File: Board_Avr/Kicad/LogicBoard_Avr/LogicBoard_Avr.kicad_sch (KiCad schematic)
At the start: 11 parts, among them J11 TriggeredStatusLedConnector, SW1 Reset switch, U1 ATmega328PB-A

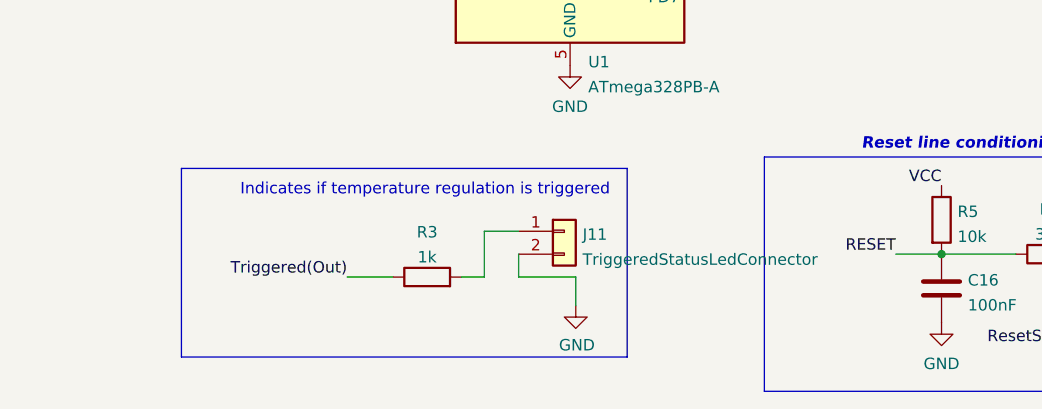
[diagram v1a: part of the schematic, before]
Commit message: Tweaked top silkscreen to embed useful information
Signed-off-by: bebenlebricolo <benoittarrade@hotmail.fr>
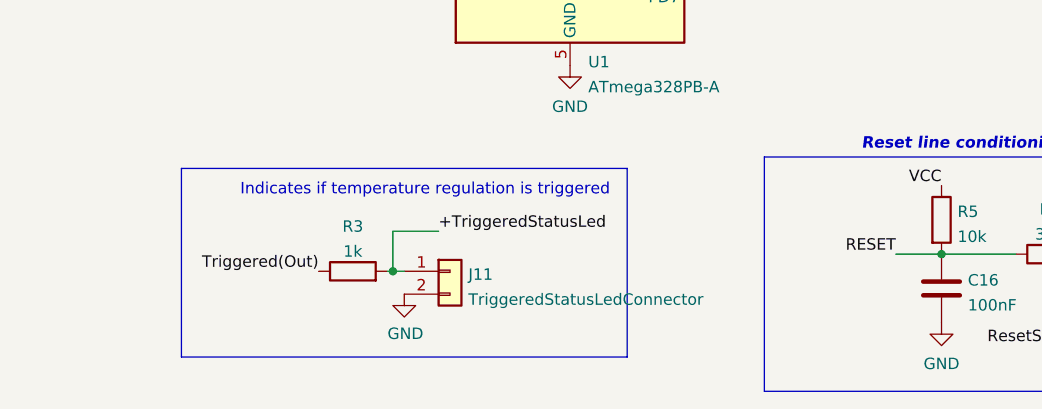
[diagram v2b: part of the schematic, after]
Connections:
- net +TriggeredStatusLed: now reaches J11.1 (Pin_1), R3.2
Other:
- moved on the sheet: J11, R3
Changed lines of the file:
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@@
 (kicad_sch (version 20211123) (generator eeschema)
   (paper "A4")
+  (junction (at 41.91 174.625) (diameter 0) (color 0 0 0 0)
+  )
   (junction (at 122.428 172.72) (diameter 0) (color 0 0 0 0)
   )
@@
     (stroke (width 0) (type default) (color 0 0 0 0))
   )
-  (wire (pts (xy 52.07 175.26) (xy 52.07 170.18))
-    (stroke (width 0) (type default) (color 0 0 0 0))
-  )
   (wire (pts (xy 256.032 77.47) (xy 259.588 77.47))
     (stroke (width 0) (type default) (color 0 0 0 0))
@@
     (stroke (width 0) (type solid) (color 0 0 0 0))
   )
-  (wire (pts (xy 52.07 170.18) (xy 55.88 170.18))
-    (stroke (width 0) (type default) (color 0 0 0 0))
-  )
   (polyline (pts (xy 242.443 46.101) (xy 242.443 42.291))
     (stroke (width 0) (type default) (color 0 0 0 0))
@@
     (stroke (width 0) (type default) (color 0 0 0 0))
   )
-  (wire (pts (xy 55.88 172.72) (xy 55.88 175.26))
-    (stroke (width 0) (type default) (color 0 0 0 0))
-  )
   (wire (pts (xy 207.645 104.775) (xy 213.487 104.775))
     (stroke (width 0) (type default) (color 0 0 0 0))
@@
     (stroke (width 0) (type default) (color 0 0 0 0))
   )
-  (wire (pts (xy 62.23 175.26) (xy 62.23 178.435))
-    (stroke (width 0) (type default) (color 0 0 0 0))
-  )
   (wire (pts (xy 213.233 53.086) (xy 206.883 53.086))
     (stroke (width 0) (type default) (color 0 0 0 0))
@@
     (stroke (width 0) (type default) (color 0 0 0 0))
   )
-  (wire (pts (xy 49.53 175.26) (xy 52.07 175.26))
-    (stroke (width 0) (type default) (color 0 0 0 0))
-  )
   (polyline (pts (xy 27.178 133.096) (xy 33.528 133.096))
     (stroke (width 0) (type solid) (color 0 0 0 0))
@@
     (stroke (width 0) (type default) (color 0 0 0 0))
   )
-  (wire (pts (xy 55.88 175.26) (xy 62.23 175.26))
+  (wire (pts (xy 41.275 174.625) (xy 41.91 174.625))
     (stroke (width 0) (type default) (color 0 0 0 0))
   )
@@
     (stroke (width 0) (type default) (color 0 0 0 0))
   )
-  (wire (pts (xy 36.83 175.26) (xy 41.91 175.26))
-    (stroke (width 0) (type default) (color 0 0 0 0))
-  )
   (wire (pts (xy 213.487 104.775) (xy 213.995 104.775))
     (stroke (width 0) (type default) (color 0 0 0 0))
@@
     (stroke (width 0) (type default) (color 0 0 0 0))
   )
+  (wire (pts (xy 41.91 174.625) (xy 43.18 174.625))
+    (stroke (width 0) (type default) (color 0 0 0 0))
+  )
   (wire (pts (xy 64.135 64.77) (xy 64.135 75.565))
     (stroke (width 0) (type default) (color 0 0 0 0))
@@
     (stroke (width 0) (type default) (color 0 0 0 0))
   )
+  (wire (pts (xy 41.91 170.18) (xy 46.99 170.18))
+    (stroke (width 0) (type default) (color 0 0 0 0))
+  )
   (polyline (pts (xy 87.63 133.096) (xy 95.758 133.096))
     (stroke (width 0) (type solid) (color 0 0 0 0))
@@
   )
   (wire (pts (xy 61.595 64.77) (xy 61.595 75.565))
+    (stroke (width 0) (type default) (color 0 0 0 0))
+  )
+  (wire (pts (xy 41.91 170.18) (xy 41.91 174.625))
     (stroke (width 0) (type default) (color 0 0 0 0))
   )
@@
     (effects (font (size 1.27 1.27)) (justify left bottom))
   )
-  (label "Triggered(Out)" (at 36.83 175.26 180)
+  (label "Triggered(Out)" (at 33.655 174.625 180)
     (effects (font (size 1.27 1.27)) (justify right bottom))
   )
@@
   (label "RESET" (at 97.79 172.72 180)
     (effects (font (size 1.27 1.27)) (justify right bottom))
+  )
+  (label "+TriggeredStatusLed" (at 46.99 170.18 0)
+    (effects (font (size 1.27 1.27)) (justify left bottom))
   )
   (label "MISO0(Prog)" (at 76.835 93.345 0)
@@
     (pin "2")
   )
-  (symbol (lib_id "power:GND") (at 62.23 178.435 0) (unit 1)
+  (symbol (lib_id "power:GND") (at 43.18 177.165 0) (unit 1)
     (in_bom yes) (on_board yes)
-    (property "Reference" "#PWR014" (id 0) (at 62.23 184.785 0)
-      (effects (font (size 1.27 1.27)) hide)
-    )
-    (property "Value" "GND" (id 1) (at 62.357 182.8292 0))
-    (property "Footprint" "" (id 2) (at 62.23 178.435 0)
-      (effects (font (size 1.27 1.27)) hide)
-    )
-    (property "Datasheet" "" (id 3) (at 62.23 178.435 0)
+    (property "Reference" "#PWR014" (id 0) (at 43.18 183.515 0)
+      (effects (font (size 1.27 1.27)) hide)
+    )
+    (property "Value" "GND" (id 1) (at 43.307 181.5592 0))
+    (property "Footprint" "" (id 2) (at 43.18 177.165 0)
+      (effects (font (size 1.27 1.27)) hide)
+    )
+    (property "Datasheet" "" (id 3) (at 43.18 177.165 0)
       (effects (font (size 1.27 1.27)) hide)
     )
@@
     (pin "2")
   )
-  (symbol (lib_id "Connector_Generic:Conn_01x02") (at 60.96 170.18 0) (unit 1)
-    (in_bom yes) (on_board yes) (fields_autoplaced)
-    (property "Reference" "J11" (id 0) (at 62.992 170.5415 0)
-      (effects (font (size 1.27 1.27)) (justify left))
-    )
-    (property "Value" "TriggeredStatusLedConnector" (id 1) (at 62.992 173.3166 0)
-      (effects (font (size 1.27 1.27)) (justify left))
-    )
-    (property "Footprint" "Connector_PinHeader_2.54mm:PinHeader_1x02_P2.54mm_Vertical" (id 2) (at 60.96 170.18 0)
-      (effects (font (size 1.27 1.27)) hide)
-    )
-    (property "Datasheet" "~" (id 3) (at 60.96 170.18 0)
+  (symbol (lib_id "Connector_Generic:Conn_01x02") (at 48.26 174.625 0) (unit 1)
+    (in_bom yes) (on_board yes) (fields_autoplaced)
+    (property "Reference" "J11" (id 0) (at 50.292 174.9865 0)
+      (effects (font (size 1.27 1.27)) (justify left))
+    )
+    (property "Value" "TriggeredStatusLedConnector" (id 1) (at 50.292 177.7616 0)
+      (effects (font (size 1.27 1.27)) (justify left))
+    )
+    (property "Footprint" "Connector_PinHeader_2.54mm:PinHeader_1x02_P2.54mm_Vertical" (id 2) (at 48.26 174.625 0)
+      (effects (font (size 1.27 1.27)) hide)
+    )
+    (property "Datasheet" "~" (id 3) (at 48.26 174.625 0)
       (effects (font (size 1.27 1.27)) hide)
     )
@@
     (pin "2")
   )
-  (symbol (lib_id "Device:R") (at 45.72 175.26 90) (unit 1)
-    (in_bom yes) (on_board yes) (fields_autoplaced)
-    (property "Reference" "R3" (id 0) (at 45.72 170.2775 90))
-    (property "Value" "1k" (id 1) (at 45.72 173.0526 90))
-    (property "Footprint" "Resistor_SMD:R_1206_3216Metric_Pad1.30x1.75mm_HandSolder" (id 2) (at 45.72 177.038 90)
-      (effects (font (size 1.27 1.27)) hide)
-    )
-    (property "Datasheet" "~" (id 3) (at 45.72 175.26 0)
-      (effects (font (size 1.27 1.27)) hide)
-    )
+  (symbol (lib_id "Device:R") (at 37.465 174.625 90) (unit 1)
+    (in_bom yes) (on_board yes) (fields_autoplaced)
+    (property "Reference" "R3" (id 0) (at 37.465 169.6425 90))
+    (property "Value" "1k" (id 1) (at 37.465 172.4176 90))
+    (property "Footprint" "Resistor_SMD:R_1206_3216Metric_Pad1.30x1.75mm_HandSolder" (id 2) (at 37.465 176.403 90)
+      (effects (font (size 1.27 1.27)) hide)
+    )
+    (property "Datasheet" "~" (id 3) (at 37.465 174.625 0)
+      (effects (font (size 1.27 1.27)) hide)
+    )

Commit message: Updated ferrite bead footprint
Signed-off-by: bebenlebricolo <benoittarrade@hotmail.fr>
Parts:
- L1: footprint Capacitor_SMD:C_0603_1608Metric -> Inductor_SMD:L_0603_1608Metric
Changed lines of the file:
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@@
     (property "Reference" "L1" (id 0) (at 48.768 59.4065 90))
     (property "Value" "BLM18AG151SN1D" (id 1) (at 48.768 61.595 90))
-    (property "Footprint" "Capacitor_SMD:C_0603_1608Metric" (id 2) (at 48.768 64.77 0)
+    (property "Footprint" "Inductor_SMD:L_0603_1608Metric" (id 2) (at 48.768 64.77 0)
       (effects (font (size 1.27 1.27)) hide)
     )
@@
     )
     (path "/dfc325fb-8de1-4eb3-b870-505e15a9d3fb"
-      (reference "L1") (unit 1) (value "BLM18AG151SN1D") (footprint "Capacitor_SMD:C_0603_1608Metric")
+      (reference "L1") (unit 1) (value "BLM18AG151SN1D") (footprint "Inductor_SMD:L_0603_1608Metric")
     )
     (path "/0e84d415-16d7-4f4e-ab35-e58625cd37e0/f4fe6211-c022-43dc-9880-a1f7b18867d5"
